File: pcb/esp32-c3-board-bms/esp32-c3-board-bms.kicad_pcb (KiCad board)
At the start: 2 copper layers, 94.9 x 40.6 mm, 32 parts, among them P101 CAN, P102 BMS UART, P3 CONN_1, P4 CONN_1, P5 CONN_1, P6 CONN_1, U102 TJA1050, U2 esp32-c3-ebay, U3 LP2985-3.3, U4 PC817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

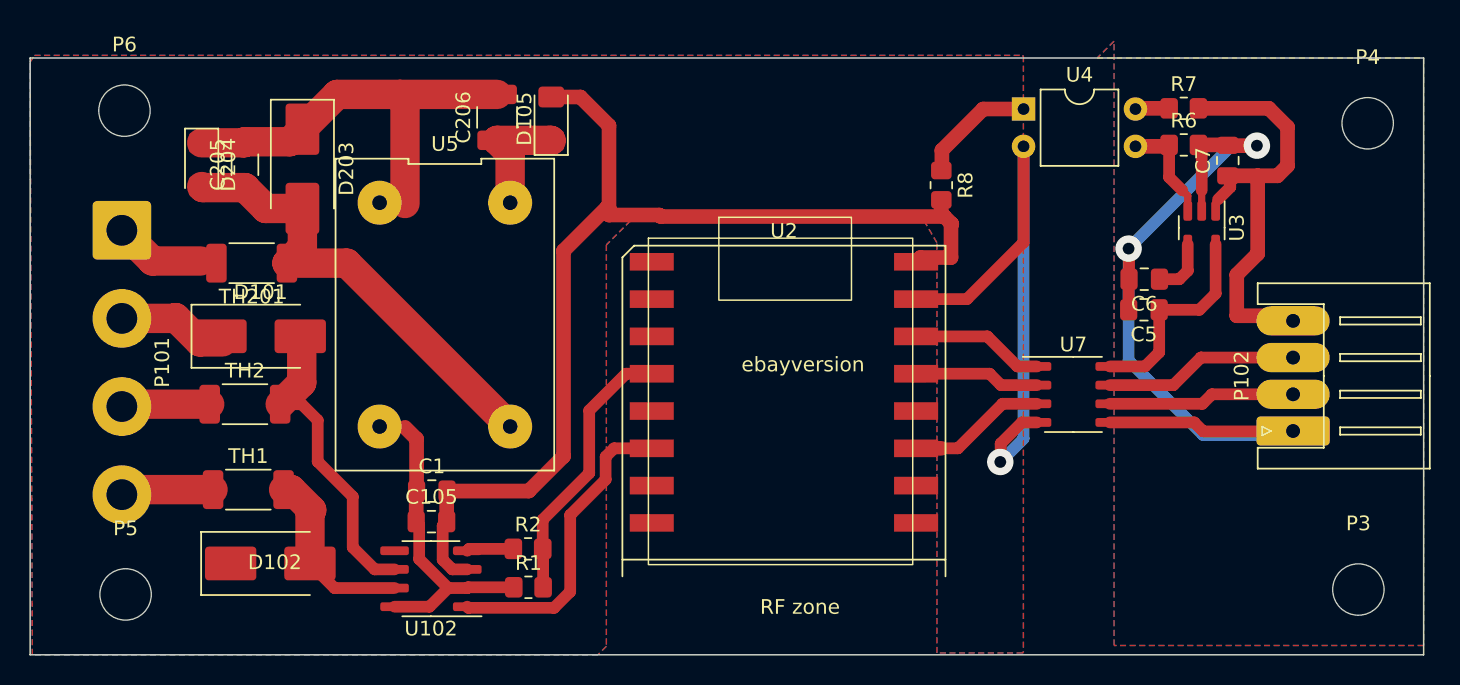
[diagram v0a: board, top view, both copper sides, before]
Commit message: Board redesigned to be isolated from the can rather than bms
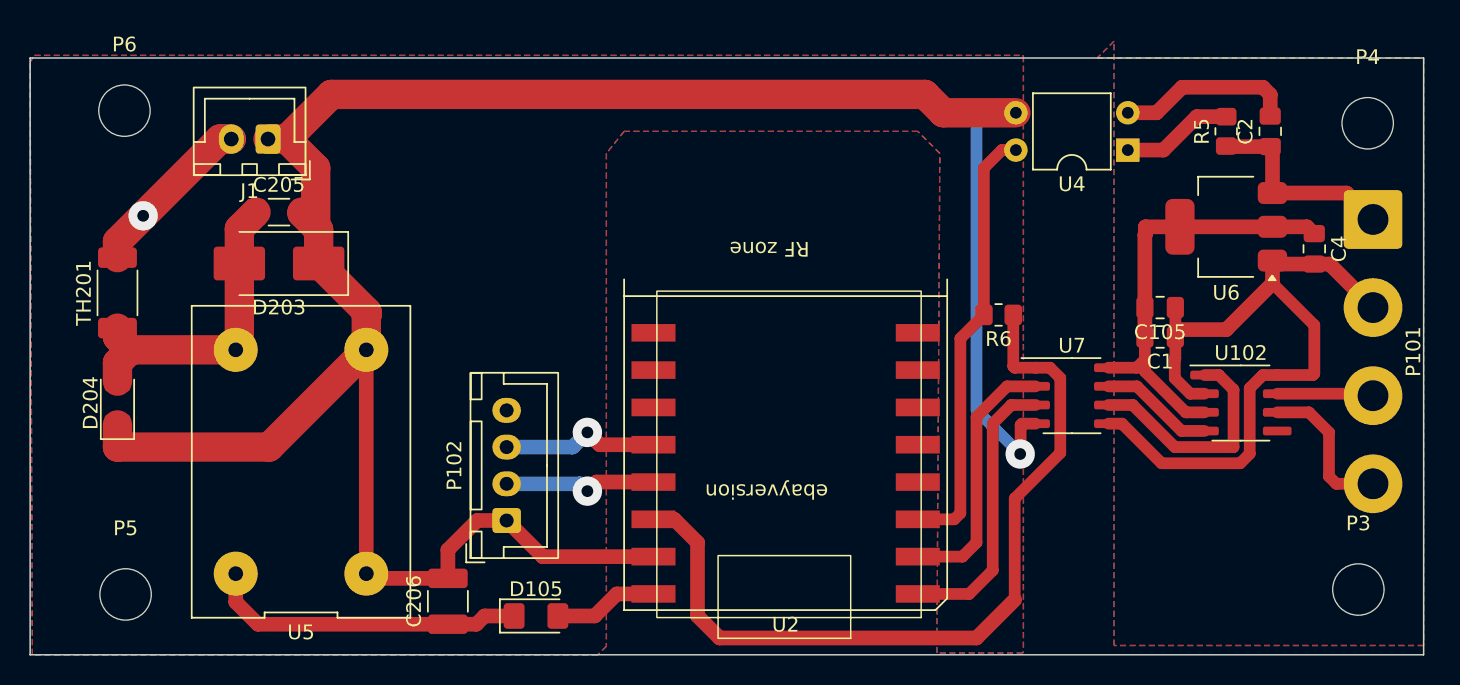
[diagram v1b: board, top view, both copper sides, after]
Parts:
- removed C5, C7: 10uF, Capacitor_SMD:C_0805_2012Metric_Pad1.18x1.45mm_HandSolder
- removed C6: 10nF, Capacitor_SMD:C_0805_2012Metric_Pad1.18x1.45mm_HandSolder
- removed D101, D102: SMBJ30CA-TR TSV, Diode_SMD:D_SMB_Handsoldering
- removed R1: 3.3K, Resistor_SMD:R_0805_2012Metric_Pad1.20x1.40mm_HandSolder
- removed R2: 2.2K, Resistor_SMD:R_0805_2012Metric_Pad1.20x1.40mm_HandSolder
- removed R7: 22K, Resistor_SMD:R_0805_2012Metric_Pad1.20x1.40mm_HandSolder
- removed R8: 10K, Resistor_SMD:R_0805_2012Metric_Pad1.20x1.40mm_HandSolder
- removed TH1, TH2: Thermistor, Resistor_SMD:R_2010_5025Metric_Pad1.40x2.65mm_HandSolder
- removed U3: LP2985-3.3, Package_TO_SOT_SMD:SOT-23-5
- added C2: 10uF, Capacitor_SMD:C_0805_2012Metric_Pad1.18x1.45mm_HandSolder, F.Cu at (121.0, 45.0)
- added C4: 10uF, Capacitor_SMD:C_0805_2012Metric_Pad1.18x1.45mm_HandSolder, F.Cu at (124.0, 53.0)
- added J1: Conn_01x02, Connector_JST:JST_XH_B2B-XH-A_1x02_P2.50mm_Vertical, F.Cu at (52.8, 45.5)
- added R5: 10K, Resistor_SMD:R_0805_2012Metric_Pad1.20x1.40mm_HandSolder, F.Cu at (118.0, 45.0)
- added U6: AMS1117-5.0, Package_TO_SOT_SMD:SOT-223-3_TabPin2, F.Cu at (118.0, 51.5)
- C1: value 10uF -> 100nF
- P102: footprint Connector_JST:JST_XH_S4B-XH-A_1x04_P2.50mm_Horizontal -> Connector_JST:JST_XH_B4B-XH-A_1x04_P2.50mm_Vertical
- moved P101 85.2 mm to (128.0, 51.0)
- moved U102 56.4 mm to (119.0, 63.5), turned to 0 degrees
- moved P102 53.9 mm to (69.0, 71.5)
- moved C105 51.7 mm to (113.5, 57.0), turned to 180 degrees
- moved C1 50.7 mm to (113.5, 59.0), turned to 180 degrees
- moved D105 33.9 mm to (71.0, 78.0), turned to 0 degrees
- moved C206 33.1 mm to (65.0, 77.0)
- moved U2 29.4 mm to (97.2, 76.5), turned to 180 degrees
- moved D204 17.2 mm to (42.5, 63.5), turned to 90 degrees
- moved R6 17.1 mm to (102.5, 57.5), turned to 180 degrees
- moved U5 14.0 mm to (55.0, 67.5), turned to 90 degrees
- moved TH201 9.36 mm to (42.5, 56.0), turned to 90 degrees
- moved U4 7.63 mm to (111.3, 46.3), turned to 180 degrees
- moved D203 6.64 mm to (53.5, 54.0), turned to 180 degrees
- moved C205 3.98 mm to (53.5, 50.5), turned to 0 degrees
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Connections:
- C1 pad 1: GND -> GND CAN
- C1 pad 2: 5V -> 5V CAN
- C105 pad 1: GND -> GND CAN
- C105 pad 2: 5V -> 5V CAN
- P101 pad 1: 12v -> 12V CAN
- P101 pad 2: GND -> GND CAN
- P101 pad 3: CAN-L -> CAN-H
- P101 pad 4: CAN-H -> CAN-L
- P102 pad 1: GND BMS -> GND
- P102 pad 2: TX to BMS -> BMS-TX
- P102 pad 3: RX from BMS -> BMS-RX
- P102 pad 4: 12V BMS -> unconnected-(P102-P4-Pad4)
- R6 pad 1: Net-(U3-ON/~{OFF}) -> 3v3
- R6 pad 2: GND BMS -> CAN-SENSE
- U102 pad 1: CAN-TX -> Net-(U102-TXD)
- U102 pad 2: GND -> GND CAN
- U102 pad 3: 5V -> 5V CAN
- U102 pad 6: Net-(D101-K) -> CAN-L
- U102 pad 7: Net-(D102-K) -> CAN-H
- U102 pad 8: GND -> GND CAN
- U2 pad 1: unconnected-(U2-gpio5-Pad1) -> CAN-TX
- U2 pad 11: BMS-TX -> unconnected-(U2-gpio2-Pad11)
- U2 pad 12: unconnected-(U2-gpio3-Pad12) -> BMS-RX
- U2 pad 13: BMS-RX -> BMS-TX
- U2 pad 2: unconnected-(U2-gop6-Pad2) -> CAN-RX
- U2 pad 3: unconnected-(U2-gpio7-Pad3) -> CAN-SENSE
- U2 pad 4: CAN-RX -> unconnected-(U2-gpio8-Pad4)
- U2 pad 6: CAN-TX -> unconnected-(U2-gpio10-Pad6)
- U4 pad 2: GND -> GND CAN
- U4 pad 3: Net-(U3-ON/~{OFF}) -> GND
- U4 pad 4: Net-(R7-Pad1) -> CAN-SENSE
- U7 pad 2: BMS-RX -> CAN-RX
- U7 pad 3: BMS-TX -> CAN-TX
- U7 pad 5: GND BMS -> GND CAN
- U7 pad 6: TX to BMS -> Net-(U102-TXD)
- U7 pad 7: RX from BMS -> Net-(U102-RXD)
- U7 pad 8: 3.3V BMS -> 5V CAN
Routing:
- net 5V: track 74.4 -> 7.13 mm
- net GND CAN: track 0.00 -> 64.6 mm
- net GND: track 99.4 -> 160.7 mm
- net GND BMS: track 58.3 -> 0.00 mm, vias 2 -> 0
- net 3v3: track 9.08 -> 55.4 mm
- net 12V BMS: track 31.2 -> 0.00 mm
- net CAN-SENSE: track 0.00 -> 29.9 mm
- net 5V CAN: track 0.00 -> 29.5 mm
- net Net-(D101-K): track 21.0 -> 0.00 mm
- net Net-(U102-TXD): track 0.00 -> 16.0 mm
- net 3.3V BMS: track 14.3 -> 0.00 mm
- net 12V CAN: track 0.00 -> 13.8 mm
- net 5.8V: track 8.31 -> 21.7 mm
- net RX from BMS: track 13.3 -> 0.00 mm
- net TX to BMS: track 12.8 -> 0.00 mm
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- added copper zone on B.Cu, net GND CAN
- added copper zone on F.Cu, net GND CAN
- removed copper zone on B.Cu, net GND BMS
- removed copper zone on F.Cu, net GND BMS

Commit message: updated board, ready for fab
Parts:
- removed D105: 1N5819, Diode_SMD:D_1206_3216Metric_Pad1.42x1.75mm_HandSolder
- added J2: Conn_01x02, Connector_JST:JST_XH_B2B-XH-A_1x02_P2.50mm_Vertical, F.Cu at (52.5, 46.0)
- moved J1 8.76 mm to (61.5, 46.0)
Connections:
- C206 pad 1: 5.8V -> 5V
- TH201 pad 2: 12v -> 12v Switched
- U5 pad 3: 5.8V -> 5V
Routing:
- net 5V: track 7.13 -> 31.9 mm
- net 5.8V: track 21.7 -> 0.00 mm
- net 12v Switched: track 0.00 -> 11.3 mm, vias 0 -> 1
- net 12v: track 12.5 -> 6.50 mm, vias 1 -> 0
- net GND: track 160.7 -> 161.1 mm, vias 1 -> 2

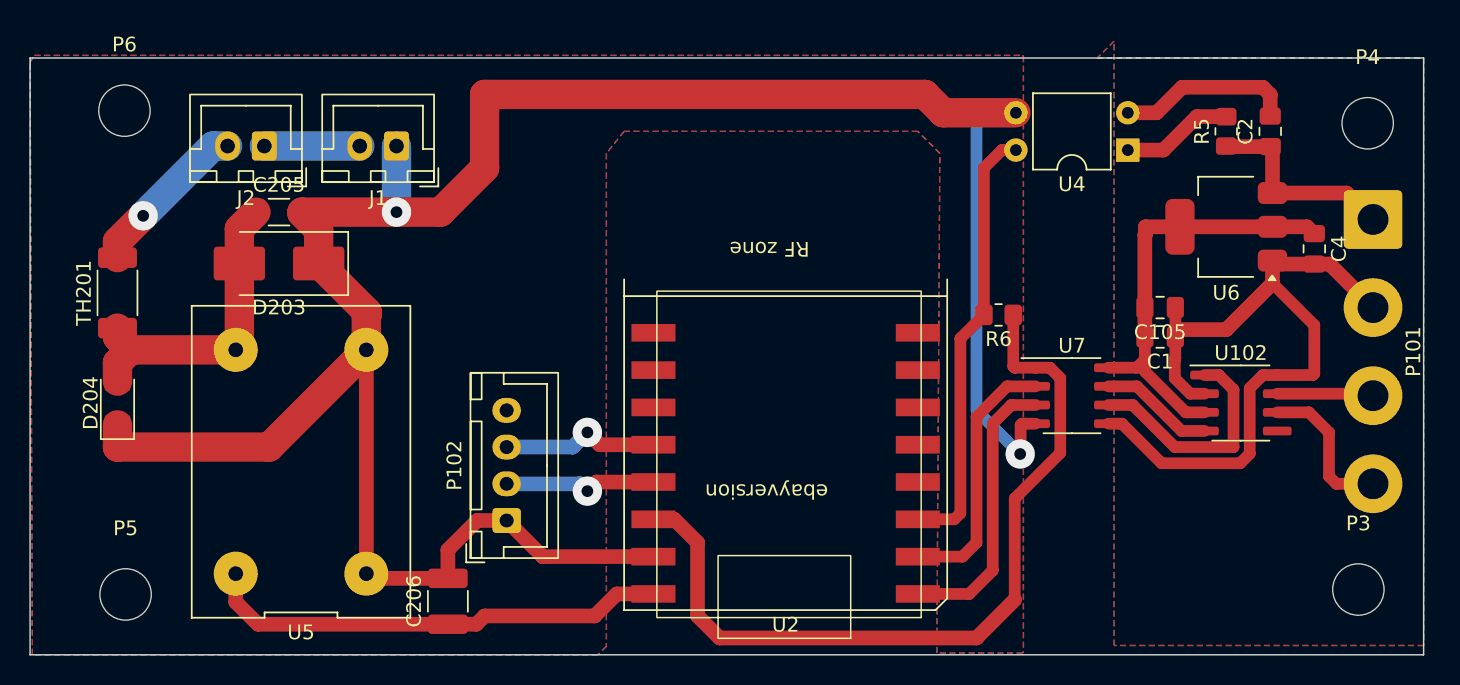
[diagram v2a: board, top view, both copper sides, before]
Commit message: onboard MP2307 DCDC
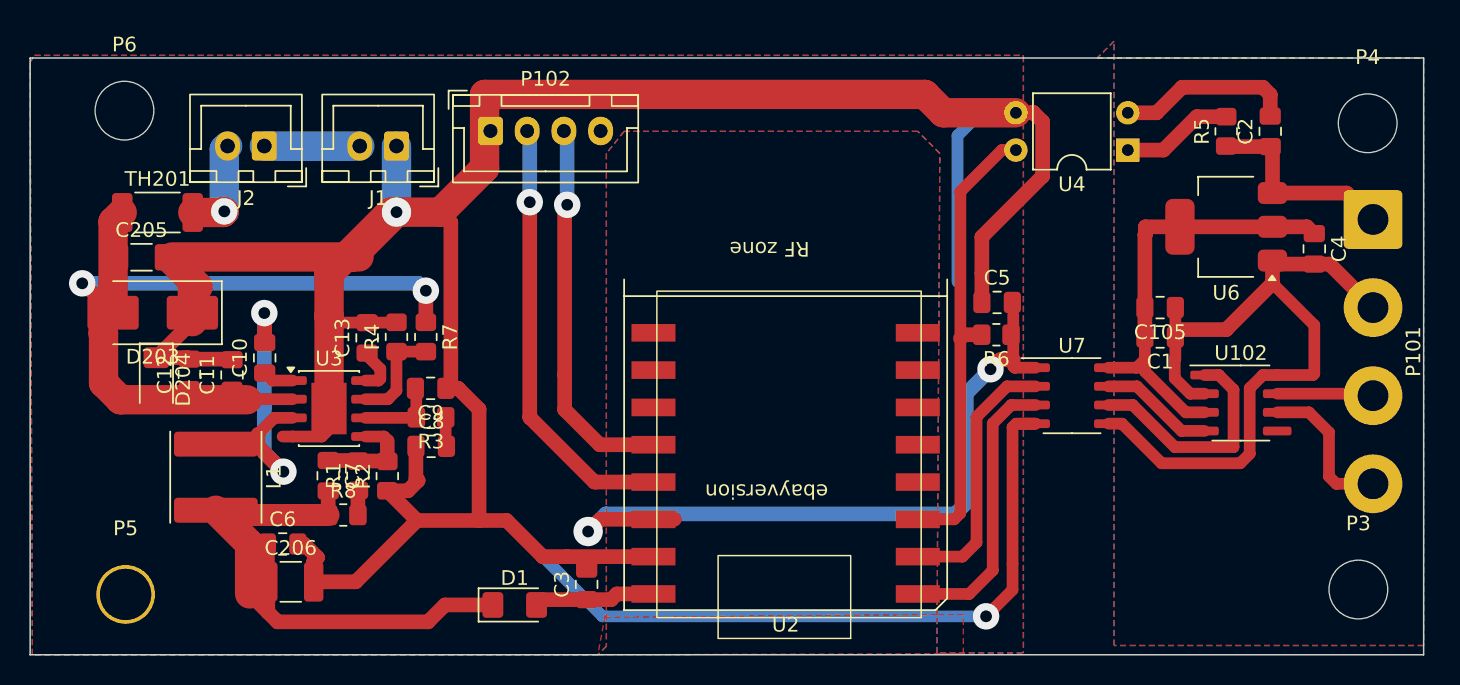
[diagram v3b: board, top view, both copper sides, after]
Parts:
- removed U5: DCDCConverter, iebSpecials:Mini360 DCDCConverter
- added C10: 10nF, Capacitor_SMD:C_0805_2012Metric_Pad1.18x1.45mm_HandSolder, F.Cu at (52.5, 60.4)
- added C11: 100nF, Capacitor_SMD:C_0805_2012Metric_Pad1.18x1.45mm_HandSolder, F.Cu at (50.3, 61.6)
- added C12: 10uF, Capacitor_SMD:C_0805_2012Metric_Pad1.18x1.45mm_HandSolder, F.Cu at (47.4, 61.5)
- added C13: 100nF, Capacitor_SMD:C_0805_2012Metric_Pad1.18x1.45mm_HandSolder, F.Cu at (59.5, 59.1)
- added C3: 10uF, Capacitor_SMD:C_0805_2012Metric_Pad1.18x1.45mm_HandSolder, F.Cu at (74.5, 75.8)
- added C5: 100nF, Capacitor_SMD:C_0805_2012Metric_Pad1.18x1.45mm_HandSolder, F.Cu at (102.4, 56.6)
- added C6: 22uF, Capacitor_SMD:C_0805_2012Metric_Pad1.18x1.45mm_HandSolder, F.Cu at (53.8, 73.1)
- added C7: 180pF, Capacitor_SMD:C_0805_2012Metric_Pad1.18x1.45mm_HandSolder, F.Cu at (56.9, 68.5)
- added C8: 6.8nF, Capacitor_SMD:C_0805_2012Metric_Pad1.18x1.45mm_HandSolder, F.Cu at (63.9, 66.5)
- added C9: 18pF, Capacitor_SMD:C_0805_2012Metric_Pad1.18x1.45mm_HandSolder, F.Cu at (63.8, 62.5)
- added D1: 1N5819, Diode_SMD:D_1206_3216Metric_Pad1.42x1.75mm_HandSolder, F.Cu at (69.5, 77.2)
- added L1: 22uH, Inductor_SMD:L_APV_ANR6045, F.Cu at (49.2, 68.5)
- added R1: 47K, Resistor_SMD:R_0805_2012Metric_Pad1.20x1.40mm_HandSolder, F.Cu at (58.9, 68.5)
- added R2: 10K, Resistor_SMD:R_0805_2012Metric_Pad1.20x1.40mm_HandSolder, F.Cu at (60.9, 68.5)
- added R3: 8.45K, Resistor_SMD:R_0805_2012Metric_Pad1.20x1.40mm_HandSolder, F.Cu at (63.9, 64.5)
- added R4: 47K, Resistor_SMD:R_0805_2012Metric_Pad1.20x1.40mm_HandSolder, F.Cu at (61.5, 59.0)
- added R7: 100K, Resistor_SMD:R_0805_2012Metric_Pad1.20x1.40mm_HandSolder, F.Cu at (63.5, 59.0)
- added R8: 1K, Resistor_SMD:R_0805_2012Metric_Pad1.20x1.40mm_HandSolder, F.Cu at (57.9, 71.1)
- added U3: MP2307, Package_SO:SOIC-8-1EP_3.9x4.9mm_P1.27mm_EP2.62x3.51mm, F.Cu at (56.9, 63.9)
- J1: value Conn_01x02 -> Power
- J2: value Conn_01x02 -> Switch
- moved P102 26.5 mm to (67.9, 45.0), turned to 0 degrees
- moved C206 10.8 mm to (54.3, 75.7), turned to 0 degrees
- moved C205 9.85 mm to (44.1, 53.6)
- moved D203 9.23 mm to (44.9, 57.4)
- moved TH201 6.12 mm to (45.2, 50.5), turned to 0 degrees
- moved D204 3.10 mm to (45.1, 61.9), turned to -90 degrees
- moved R6 1.36 mm to (102.3, 58.9)
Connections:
- C206 pad 1: 5V -> 5.5V
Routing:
- net GND: track 161.1 -> 251.7 mm
- net 5.5V: track 0.00 -> 39.8 mm
- net 12vFused: track 21.5 -> 52.5 mm, vias 0 -> 2
- net 5V: track 31.9 -> 8.27 mm
- net Net-(U3-SW): track 0.00 -> 22.6 mm, vias 0 -> 2
- net BMS-TX: track 10.5 -> 29.8 mm
- net BMS-RX: track 10.8 -> 26.2 mm
- net Net-(U3-FB): track 0.00 -> 7.15 mm
- net Net-(U3-EN): track 0.00 -> 7.01 mm
- net 3v3: track 55.4 -> 49.4 mm, vias 0 -> 2
- net Net-(U3-COMP): track 0.00 -> 5.48 mm
- net 12v Switched: track 11.3 -> 6.72 mm
- net Net-(U3-SS): track 0.00 -> 3.35 mm
- net Net-(U3-BS): track 0.00 -> 2.11 mm
- net Net-(C8-Pad2): track 0.00 -> 2.00 mm
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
